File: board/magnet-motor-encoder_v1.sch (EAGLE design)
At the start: 12 parts, among them IC1 AS5045B

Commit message: board layout and silkscreen
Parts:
- LED_BLUE: value BLUE -> POWER
- LED_RED: value RED -> DEC
- LED_YELLOW: value YELLOW -> INC
- R1, R2: value 330 -> 1k
- SJ1: value 5V? -> 3V3?
- renumbered LED1 to LED_YELLOW, LED2 to LED_RED, LED3 to LED_BLUE
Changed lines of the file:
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@@
 <part name="IC1" library="austriamicrosystems" deviceset="AS5040" device="" value="AS5045B"/>
 <part name="FRAME1" library="rca_templates" deviceset="FRAME_A4L" device=""/>
-<part name="LED1" library="led" deviceset="LED" device="CHIPLED_0805" value="YELLOW"/>
-<part name="LED2" library="led" deviceset="LED" device="CHIPLED_0805" value="RED"/>
-<part name="LED3" library="led" deviceset="LED" device="CHIPLED_0805" value="BLUE"/>
-<part name="R1" library="resistor" deviceset="R-EU_" device="R0805" value="330"/>
-<part name="R2" library="resistor" deviceset="R-EU_" device="R0805" value="330"/>
+<part name="LED_YELLOW" library="led" deviceset="LED" device="CHIPLED_0805" value="INC"/>
+<part name="LED_RED" library="led" deviceset="LED" device="CHIPLED_0805" value="DEC"/>
+<part name="LED_BLUE" library="led" deviceset="LED" device="CHIPLED_0805" value="POWER"/>
+<part name="R1" library="resistor" deviceset="R-EU_" device="R0805" value="1k"/>
+<part name="R2" library="resistor" deviceset="R-EU_" device="R0805" value="1k"/>
 <part name="R3" library="resistor" deviceset="R-EU_" device="R0805" value="1k"/>
 <part name="C1" library="resistor" deviceset="C-EU" device="C0805K" value="100n"/>
 <part name="C2" library="resistor" deviceset="C-EU" device="C0805K" value="10µ"/>
-<part name="SJ1" library="rca_sontiges" deviceset="SJ" device="S" value="5V?"/>
+<part name="SJ1" library="rca_sontiges" deviceset="SJ" device="S" value="3V3?"/>
 <part name="GND1" library="rca_sontiges" deviceset="GND" device=""/>
 <part name="P+1" library="supply1" deviceset="+5V" device=""/>
@@
 <instance part="IC1" gate="G$1" x="0" y="0"/>
 <instance part="FRAME1" gate="G$1" x="-157.48" y="-88.9"/>
-<instance part="LED1" gate="G$1" x="-27.94" y="20.32"/>
-<instance part="LED2" gate="G$1" x="-43.18" y="20.32"/>
-<instance part="LED3" gate="G$1" x="-66.04" y="20.32"/>
+<instance part="LED_YELLOW" gate="G$1" x="-27.94" y="20.32"/>
+<instance part="LED_RED" gate="G$1" x="-43.18" y="20.32"/>
+<instance part="LED_BLUE" gate="G$1" x="-66.04" y="20.32"/>
 <instance part="R1" gate="G$1" x="-27.94" y="30.48" rot="R90"/>
 <instance part="R2" gate="G$1" x="-43.18" y="30.48" rot="R90"/>
@@
 <net name="LED_RED" class="0">
 <segment>
-<pinref part="LED2" gate="G$1" pin="C"/>
+<pinref part="LED_RED" gate="G$1" pin="C"/>
 <pinref part="IC1" gate="G$1" pin="MAGDEC"/>
 <wire x1="-43.18" y1="15.24" x2="-43.18" y2="5.08" width="0.1524" layer="91"/>
@@
 <segment>
 <pinref part="IC1" gate="G$1" pin="MAGINC"/>
-<pinref part="LED1" gate="G$1" pin="C"/>
+<pinref part="LED_YELLOW" gate="G$1" pin="C"/>
 <wire x1="-17.78" y1="7.62" x2="-27.94" y2="7.62" width="0.1524" layer="91"/>
 <wire x1="-27.94" y1="7.62" x2="-27.94" y2="15.24" width="0.1524" layer="91"/>
@@
 <segment>
 <pinref part="R1" gate="G$1" pin="1"/>
-<pinref part="LED1" gate="G$1" pin="A"/>
+<pinref part="LED_YELLOW" gate="G$1" pin="A"/>
 <wire x1="-27.94" y1="25.4" x2="-27.94" y2="22.86" width="0.1524" layer="91"/>
 </segment>
@@
 <segment>
 <pinref part="R2" gate="G$1" pin="1"/>
-<pinref part="LED2" gate="G$1" pin="A"/>
+<pinref part="LED_RED" gate="G$1" pin="A"/>
 <wire x1="-43.18" y1="25.4" x2="-43.18" y2="22.86" width="0.1524" layer="91"/>
 </segment>
@@
 <segment>
 <pinref part="R3" gate="G$1" pin="1"/>
-<pinref part="LED3" gate="G$1" pin="A"/>
+<pinref part="LED_BLUE" gate="G$1" pin="A"/>
 <wire x1="-66.04" y1="25.4" x2="-66.04" y2="22.86" width="0.1524" layer="91"/>
 </segment>
@@
 <segment>
 <pinref part="GND3" gate="1" pin="GND"/>
-<pinref part="LED3" gate="G$1" pin="C"/>
+<pinref part="LED_BLUE" gate="G$1" pin="C"/>
 <wire x1="-66.04" y1="10.16" x2="-66.04" y2="15.24" width="0.1524" layer="91"/>
 </segment>

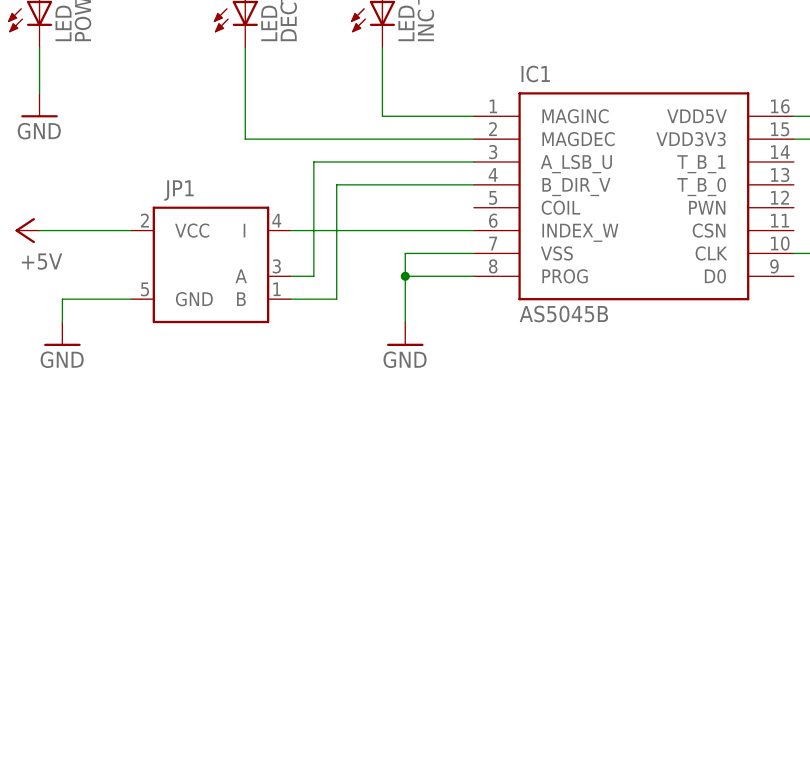
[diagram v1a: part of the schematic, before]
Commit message: board: add DS18B20 temperature sensor (optional/uses encoder index pin signal)
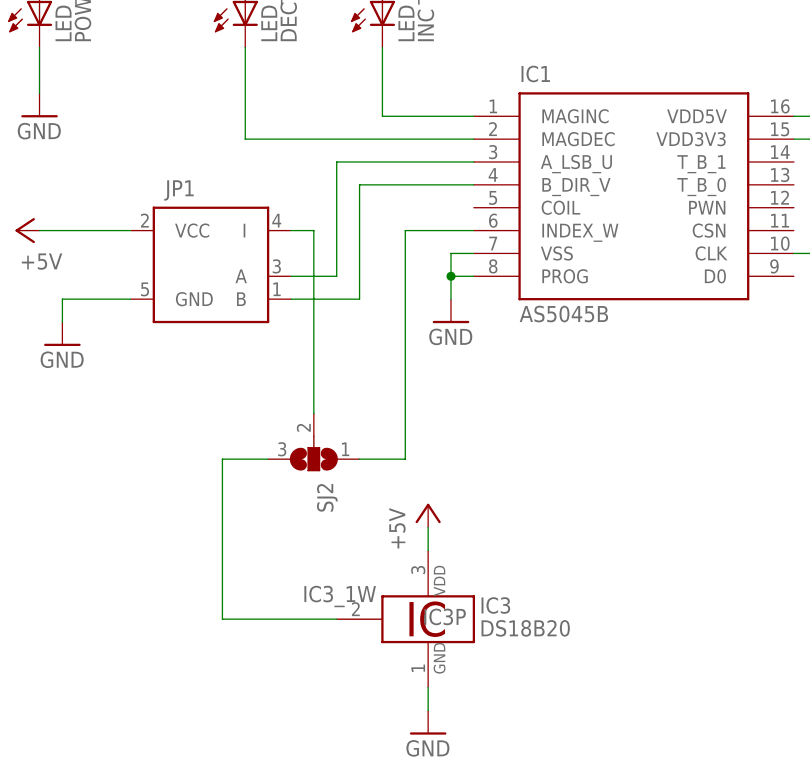
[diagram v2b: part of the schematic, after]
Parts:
- added IC3: DS18B20, 1wire:DS18S20
- added SJ2: (no value), jumper:SJ2W
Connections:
- removed net INDEX: IC1.INDEX_W, JP1.I
- new net N$1: JP1.I, SJ2.2
- new net N$2: IC1.INDEX_W, SJ2.1
- new net N$3: IC3_1W.1W, SJ2.3
- net +5V: now also IC3P.VDD
- net GND: now also IC3P.GND
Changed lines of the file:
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@@
 <part name="P+5" library="supply1" deviceset="+5V" device=""/>
 <part name="P+6" library="supply1" deviceset="+5V" device=""/>
+<part name="SJ2" library="jumper" deviceset="SJ2W" device=""/>
+<part name="IC3" library="1wire" deviceset="DS18S20" device="" value="DS18B20"/>
+<part name="GND6" library="rca_sontiges" deviceset="GND" device=""/>
+<part name="P+7" library="supply1" deviceset="+5V" device=""/>
 </parts>
 <sheets>
@@
 <instance part="C2" gate="G$1" x="-91.44" y="-48.26" rot="R180"/>
 <instance part="SJ1" gate="1" x="-106.68" y="-40.64"/>
-<instance part="GND1" gate="1" x="-25.4" y="-17.78"/>
+<instance part="GND1" gate="1" x="-20.32" y="-15.24"/>
 <instance part="P+1" gate="1" x="33.02" y="17.78"/>
 <instance part="+3V1" gate="G$1" x="40.64" y="17.78"/>
@@
 <instance part="P+5" gate="1" x="-43.18" y="45.72"/>
 <instance part="P+6" gate="1" x="-27.94" y="45.72"/>
+<instance part="SJ2" gate="G$1" x="-35.56" y="-30.48" rot="R270"/>
+<instance part="IC3" gate="A" x="-22.86" y="-48.26"/>
+<instance part="IC3" gate="P" x="-22.86" y="-48.26"/>
+<instance part="IC3" gate="_1W" x="-27.94" y="-48.26"/>
+<instance part="GND6" gate="1" x="-22.86" y="-60.96"/>
+<instance part="P+7" gate="1" x="-22.86" y="-35.56"/>
 </instances>
 <busses>
@@
 <wire x1="-27.94" y1="43.18" x2="-27.94" y2="35.56" width="0.1524" layer="91"/>
 </segment>
+<segment>
+<pinref part="P+7" gate="1" pin="+5V"/>
+<pinref part="IC3" gate="P" pin="VDD"/>
+<wire x1="-22.86" y1="-38.1" x2="-22.86" y2="-40.64" width="0.1524" layer="91"/>
+</segment>
 </net>
 <net name="+3V3" class="0">
@@
 <pinref part="IC1" gate="G$1" pin="VSS"/>
 <pinref part="GND1" gate="1" pin="GND"/>
-<wire x1="-17.78" y1="-7.62" x2="-25.4" y2="-7.62" width="0.1524" layer="91"/>
-<wire x1="-25.4" y1="-7.62" x2="-25.4" y2="-10.16" width="0.1524" layer="91"/>
+<wire x1="-17.78" y1="-7.62" x2="-20.32" y2="-7.62" width="0.1524" layer="91"/>
+<wire x1="-20.32" y1="-7.62" x2="-20.32" y2="-10.16" width="0.1524" layer="91"/>
 <pinref part="IC1" gate="G$1" pin="PROG"/>
-<wire x1="-25.4" y1="-10.16" x2="-25.4" y2="-15.24" width="0.1524" layer="91"/>
-<wire x1="-17.78" y1="-10.16" x2="-25.4" y2="-10.16" width="0.1524" layer="91"/>
-<junction x="-25.4" y="-10.16"/>
+<wire x1="-20.32" y1="-10.16" x2="-20.32" y2="-12.7" width="0.1524" layer="91"/>
+<wire x1="-17.78" y1="-10.16" x2="-20.32" y2="-10.16" width="0.1524" layer="91"/>
+<junction x="-20.32" y="-10.16"/>
 </segment>
 <segment>
@@
 <wire x1="27.94" y1="-7.62" x2="17.78" y2="-7.62" width="0.1524" layer="91"/>
 </segment>
-</net>
-<net name="INDEX" class="0">
-<segment>
+<segment>
+<pinref part="GND6" gate="1" pin="GND"/>
+<pinref part="IC3" gate="P" pin="GND"/>
+<wire x1="-22.86" y1="-58.42" x2="-22.86" y2="-55.88" width="0.1524" layer="91"/>
+</segment>
+</net>
+<net name="A" class="0">
+<segment>
+<pinref part="JP1" gate="G$1" pin="A"/>
+<wire x1="-38.1" y1="-10.16" x2="-33.02" y2="-10.16" width="0.1524" layer="91"/>
+<wire x1="-33.02" y1="-10.16" x2="-33.02" y2="2.54" width="0.1524" layer="91"/>
+<pinref part="IC1" gate="G$1" pin="A_LSB_U"/>
+<wire x1="-33.02" y1="2.54" x2="-17.78" y2="2.54" width="0.1524" layer="91"/>
+</segment>
+</net>
+<net name="B" class="0">
+<segment>
+<pinref part="JP1" gate="G$1" pin="B"/>
+<wire x1="-38.1" y1="-12.7" x2="-30.48" y2="-12.7" width="0.1524" layer="91"/>
+<wire x1="-30.48" y1="-12.7" x2="-30.48" y2="0" width="0.1524" layer="91"/>
+<pinref part="IC1" gate="G$1" pin="B_DIR_V"/>
+<wire x1="-30.48" y1="0" x2="-17.78" y2="0" width="0.1524" layer="91"/>
+</segment>
+</net>
+<net name="N$1" class="0">
+<segment>
+<pinref part="SJ2" gate="G$1" pin="2"/>
+<wire x1="-35.56" y1="-25.4" x2="-35.56" y2="-5.08" width="0.1524" layer="91"/>
 <pinref part="JP1" gate="G$1" pin="I"/>
+<wire x1="-35.56" y1="-5.08" x2="-38.1" y2="-5.08" width="0.1524" layer="91"/>
+</segment>
+</net>
+<net name="N$2" class="0">
+<segment>
+<pinref part="SJ2" gate="G$1" pin="1"/>
+<wire x1="-30.48" y1="-30.48" x2="-25.4" y2="-30.48" width="0.1524" layer="91"/>
+<wire x1="-25.4" y1="-30.48" x2="-25.4" y2="-5.08" width="0.1524" layer="91"/>
 <pinref part="IC1" gate="G$1" pin="INDEX_W"/>
-<wire x1="-38.1" y1="-5.08" x2="-17.78" y2="-5.08" width="0.1524" layer="91"/>
-</segment>
-</net>
-<net name="A" class="0">
-<segment>
-<pinref part="JP1" gate="G$1" pin="A"/>
-<wire x1="-38.1" y1="-10.16" x2="-35.56" y2="-10.16" width="0.1524" layer="91"/>
-<wire x1="-35.56" y1="-10.16" x2="-35.56" y2="2.54" width="0.1524" layer="91"/>
-<pinref part="IC1" gate="G$1" pin="A_LSB_U"/>
-<wire x1="-35.56" y1="2.54" x2="-17.78" y2="2.54" width="0.1524" layer="91"/>
-</segment>
-</net>
-<net name="B" class="0">
-<segment>
-<pinref part="JP1" gate="G$1" pin="B"/>
-<wire x1="-38.1" y1="-12.7" x2="-33.02" y2="-12.7" width="0.1524" layer="91"/>
-<wire x1="-33.02" y1="-12.7" x2="-33.02" y2="0" width="0.1524" layer="91"/>
-<pinref part="IC1" gate="G$1" pin="B_DIR_V"/>
-<wire x1="-33.02" y1="0" x2="-17.78" y2="0" width="0.1524" layer="91"/>
-</segment>
-</net>
+<wire x1="-25.4" y1="-5.08" x2="-17.78" y2="-5.08" width="0.1524" layer="91"/>
+</segment>
+</net>
+<net name="N$3" class="0">
+<segment>
+<pinref part="IC3" gate="_1W" pin="1W"/>
+<wire x1="-33.02" y1="-48.26" x2="-45.72" y2="-48.26" width="0.1524" layer="91"/>
+<wire x1="-45.72" y1="-48.26" x2="-45.72" y2="-30.48" width="0.1524" layer="91"/>
+<pinref part="SJ2" gate="G$1" pin="3"/>
+<wire x1="-45.72" y1="-30.48" x2="-40.64" y2="-30.48" width="0.1524" layer="91"/>
+</segment>
+</net>

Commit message: board: adjust silk screen; add rev2 label
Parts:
- SJ2: value (none) -> IDX / TEMP
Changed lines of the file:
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@@
 <part name="P+5" library="supply1" deviceset="+5V" device=""/>
 <part name="P+6" library="supply1" deviceset="+5V" device=""/>
-<part name="SJ2" library="jumper" deviceset="SJ2W" device=""/>
+<part name="SJ2" library="jumper" deviceset="SJ2W" device="" value="IDX / TEMP"/>
 <part name="IC3" library="1wire" deviceset="DS18S20" device="" value="DS18B20"/>
 <part name="GND6" library="rca_sontiges" deviceset="GND" device=""/>
